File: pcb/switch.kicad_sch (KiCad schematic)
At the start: 6 parts, among them J23 JST-XH

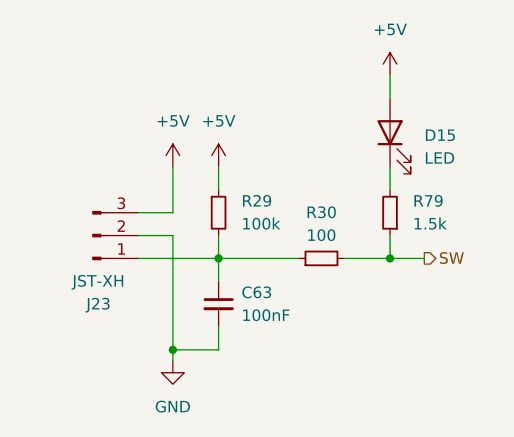
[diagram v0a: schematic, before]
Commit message: fixes #8: changed led series resistor values
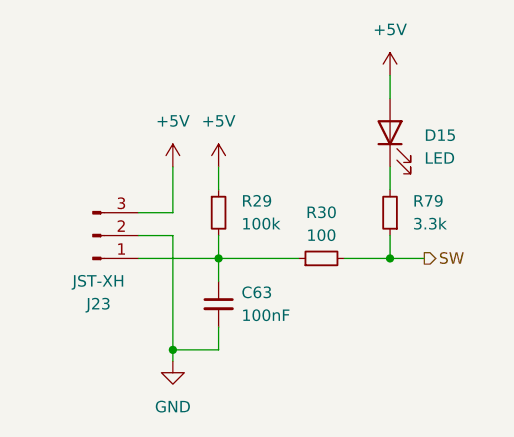
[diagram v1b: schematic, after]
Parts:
- R79: value 1.5k -> 3.3k
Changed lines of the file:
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@@
 		(fields_autoplaced yes)
 		(property "Reference" "R79"
-			(at 105.41 52.07 0)
+			(at 105.41 52.0699 0)
 			(effects
 				(font
@@
 			)
 		)
-		(property "Value" "1.5k"
-			(at 105.41 54.61 0)
+		(property "Value" "3.3k"
+			(at 105.41 54.6099 0)
 			(effects
 				(font

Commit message: specified some values and colors added lcsc part ids for all components
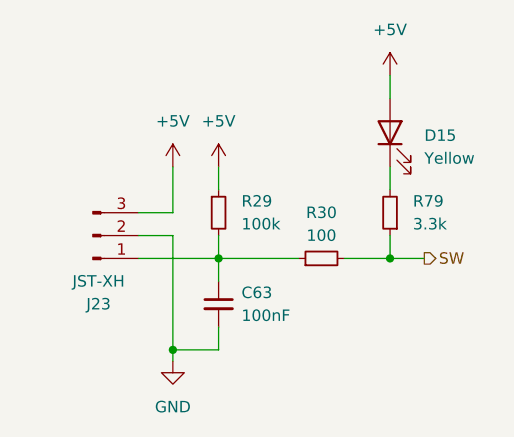
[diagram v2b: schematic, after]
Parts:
- C63: LCSC (none) -> C14663
- D15: value LED -> Yellow; LCSC (none) -> C72038
- J23: LCSC (none) -> C565985
- R29: LCSC (none) -> C14675
- R30: LCSC (none) -> C105588
- R79: LCSC (none) -> C22978
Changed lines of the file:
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@@
+			)
+		)
+		(property "LCSC" "C105588"
+			(at 95.25 53.34 0)
+			(effects
+				(font
+					(size 1.27 1.27)
+				)
+				(hide yes)
 			)
 		)
@@
 		(fields_autoplaced yes)
 		(property "Reference" "D15"
-			(at 106.68 44.7675 90)
+			(at 106.68 44.7674 90)
 			(effects
 				(font
@@
 			)
 		)
-		(property "Value" "LED"
-			(at 106.68 47.3075 90)
+		(property "Value" "Yellow"
+			(at 106.68 47.3074 90)
 			(effects
 				(font
@@
 		(property "Description" "Light emitting diode"
 			(at 102.87 44.45 0)
+			(effects
+				(font
+					(size 1.27 1.27)
+				)
+				(hide yes)
+			)
+		)
+		(property "LCSC" "C72038"
+			(at 106.68 44.7674 0)
 			(effects
 				(font
@@
 			)
 		)
+		(property "LCSC" "C22978"
+			(at 105.41 52.0699 0)
+			(effects
+				(font
+					(size 1.27 1.27)
+				)
+				(hide yes)
+			)
+		)
 		(pin "1"
 		)
@@
 			)
 		)
+		(property "LCSC" "C565985"
+			(at 70.485 63.5 0)
+			(effects
+				(font
+					(size 1.27 1.27)
+				)
+				(hide yes)
+			)
+		)
 		(pin "2"
 		)
@@
 			)
 		)
+		(property "LCSC" "C14675"
+			(at 86.36 52.07 0)
+			(effects
+				(font
+					(size 1.27 1.27)
+				)
+				(hide yes)
+			)
+		)
 		(pin "1"
 		)
@@
 			(effects
 				(font
+					(size 1.27 1.27)
+				)
+				(hide yes)
+			)
+		)
+		(property "LCSC" "C14663"
+			(at 86.36 62.2363 0)
+			(effects
+				(font

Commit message: fixes #20 fixes #22 fixes #19
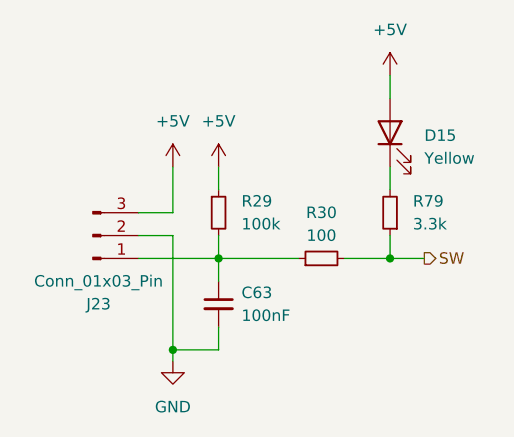
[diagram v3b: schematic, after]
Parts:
- J23: value JST-XH -> Conn_01x03_Pin
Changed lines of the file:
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@@
 			)
 		)
-		(property "Value" "JST-XH"
+		(property "Value" "Conn_01x03_Pin"
 			(at 70.485 60.96 0)
 			(effects
